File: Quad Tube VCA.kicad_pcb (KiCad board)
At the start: 2 copper layers, 162.6 x 100.3 mm, 212 parts, among them IC1 TL072, IC2 LM358, IC3 TL072, IC4 LM358, IC5 TL072, IC6 LM358, IC7 TL072, IC8 LM358

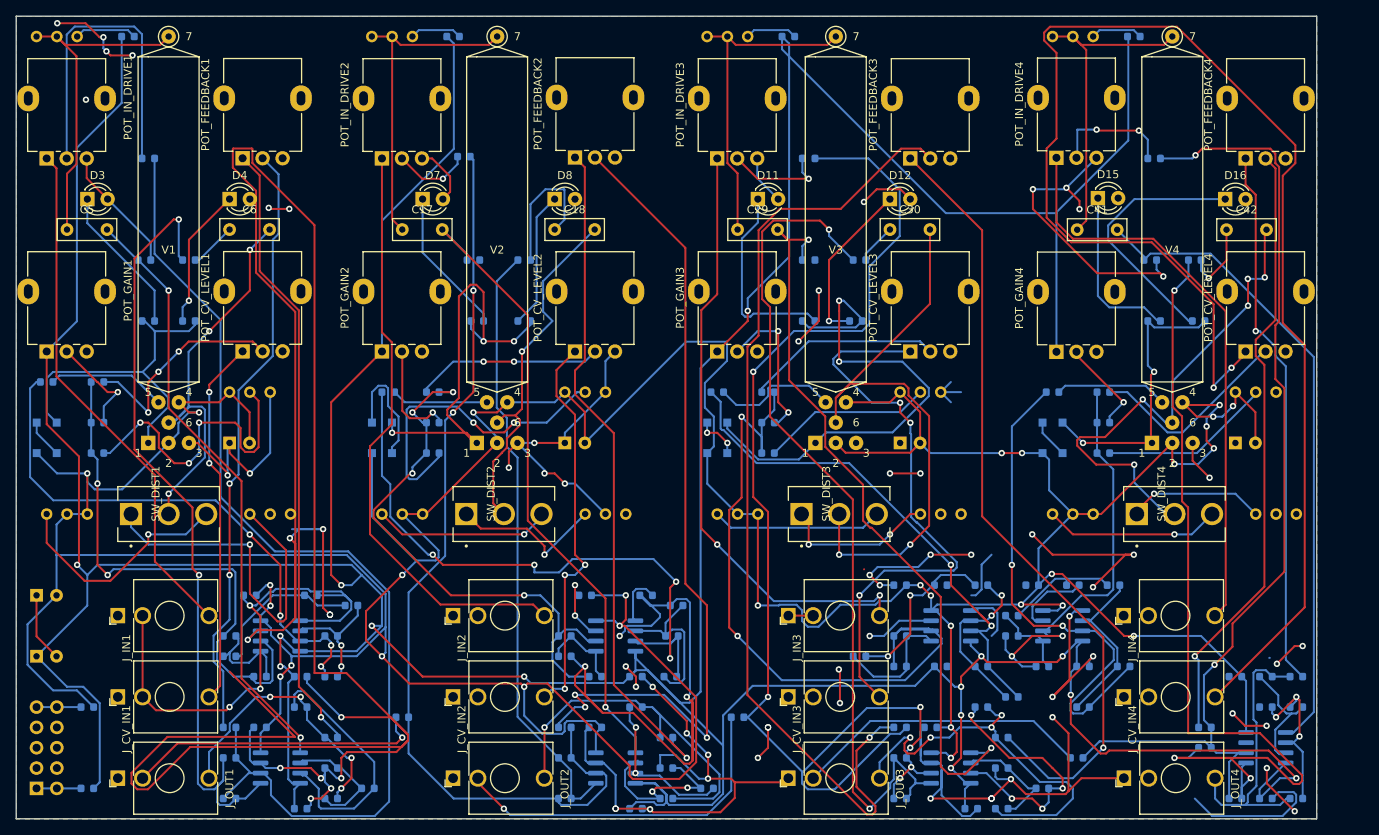
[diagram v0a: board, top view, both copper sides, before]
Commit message: power and vca1 routed
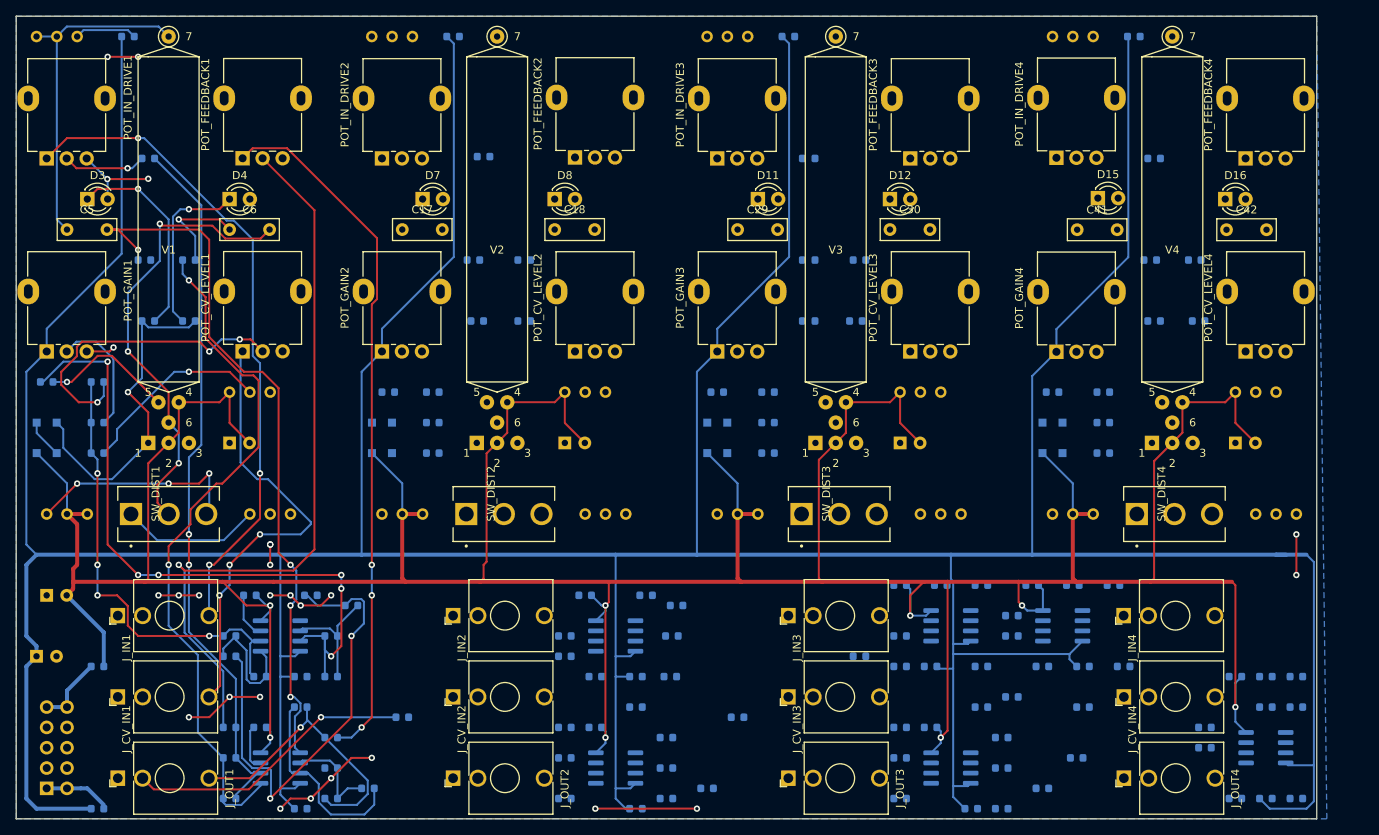
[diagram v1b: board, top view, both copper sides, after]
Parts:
- moved FB2 5.24 mm to (76.2, 125.7)
- moved FB1 2.84 mm to (76.2, 143.5), turned to 180 degrees
- moved R27 2.46 mm to (124.5, 62.0)
- moved C35 1.27 mm to (180.3, 125.7), turned to 180 degrees
- moved C3 1.27 mm to (69.8, 116.8)
- moved JP1 1.27 mm to (69.8, 141.0)
- turned R3 to 180 degrees
- turned R5 to 180 degrees
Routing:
- net GND: track 852.1 -> 88.2 mm, vias 74 -> 26
- net Net-(J_CV_IN4-Pad3): track 179.5 -> 0.00 mm, vias 2 -> 0
- net Net-(C27-Pad2): track 155.0 -> 0.00 mm, vias 6 -> 0
- net -12V: track 649.3 -> 523.6 mm, vias 30 -> 8
- net Net-(C39-Pad2): track 123.8 -> 0.00 mm, vias 2 -> 0
- net Net-(POT_FEEDBACK3-Pad2): track 121.7 -> 0.00 mm, vias 1 -> 0
- net Net-(C39-Pad1): track 117.2 -> 0.00 mm, vias 3 -> 0
- net Net-(C15-Pad2): track 117.2 -> 0.00 mm, vias 2 -> 0
- net Net-(C27-Pad1): track 108.4 -> 0.00 mm, vias 2 -> 0
- net Net-(POT_FEEDBACK2-Pad2): track 103.7 -> 0.00 mm, vias 3 -> 0
- net Net-(POT_FEEDBACK3-Pad1): track 99.2 -> 0.00 mm, vias 1 -> 0
- net Net-(C29-Pad2): track 93.8 -> 0.00 mm, vias 2 -> 0
- net Net-(C33-Pad1): track 88.4 -> 0.00 mm, vias 2 -> 0
- net Net-(POT_FEEDBACK2-Pad1): track 85.1 -> 0.00 mm, vias 1 -> 0
- net Net-(C20-Pad2): track 81.2 -> 0.00 mm, vias 4 -> 0
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
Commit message: changes footprints for pots/jacks
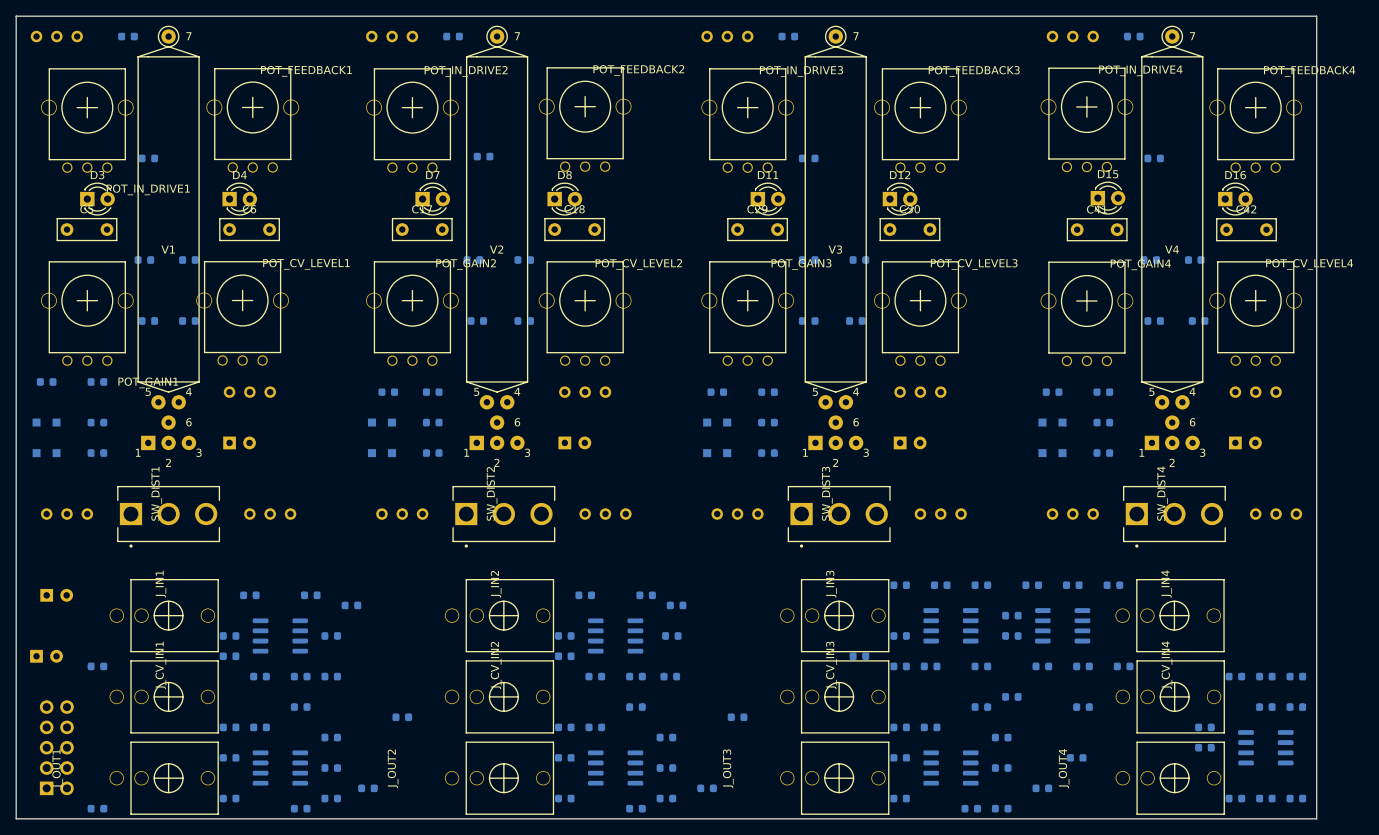
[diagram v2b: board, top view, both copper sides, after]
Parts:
- J_CV_IN1, J_CV_IN2, J_CV_IN3, J_CV_IN4, J_IN1, J_IN2, J_IN3, J_IN4, J_OUT1, J_OUT2, J_OUT3, J_OUT4: footprint Connector_Audio:Jack_3.5mm_QingPu_WQP-PJ398SM_Vertical_CircularHoles -> Eurocad:PJ301M-12
- POT_CV_LEVEL1, POT_CV_LEVEL2, POT_CV_LEVEL3, POT_CV_LEVEL4, POT_FEEDBACK1, POT_FEEDBACK2, POT_FEEDBACK3, POT_FEEDBACK4, POT_GAIN1, POT_GAIN2, POT_GAIN3, POT_GAIN4, POT_IN_DRIVE1, POT_IN_DRIVE2, POT_IN_DRIVE3, POT_IN_DRIVE4: footprint Potentiometer_THT:Potentiometer_Alpha_RD901F-40-00D_Single_Vertical -> Eurocad:Alpha9mmPot
- moved POT_GAIN1 8.13 mm to (74.9, 80.0), turned to 0 degrees
- moved POT_IN_DRIVE1 8.13 mm to (74.9, 55.9), turned to 0 degrees
- moved POT_GAIN4 7.41 mm to (199.9, 80.0), turned to 0 degrees
- moved POT_IN_DRIVE4 7.41 mm to (199.9, 55.8), turned to 0 degrees
- moved POT_GAIN3 7.41 mm to (157.5, 80.0), turned to 0 degrees
- moved POT_IN_DRIVE3 7.41 mm to (157.5, 55.9), turned to 0 degrees
- moved POT_GAIN2 7.41 mm to (115.6, 80.0), turned to 0 degrees
- moved POT_IN_DRIVE2 7.41 mm to (115.6, 55.9), turned to 0 degrees
- moved POT_FEEDBACK2 6.48 mm to (137.2, 55.8), turned to 0 degrees
- moved POT_FEEDBACK1 6.48 mm to (95.6, 55.9), turned to 0 degrees
- moved POT_CV_LEVEL2 6.48 mm to (137.2, 80.0), turned to 0 degrees
- moved POT_CV_LEVEL3 6.48 mm to (179.1, 80.0), turned to 0 degrees
- moved POT_CV_LEVEL4 6.48 mm to (221.0, 80.0), turned to 0 degrees
- moved POT_FEEDBACK3 6.48 mm to (179.1, 55.9), turned to 0 degrees
- moved POT_FEEDBACK4 6.48 mm to (221.0, 55.9), turned to 0 degrees
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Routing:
- net +12V: track 663.4 -> 0.00 mm
- net -12V: track 523.6 -> 0.00 mm, vias 8 -> 0
- net Net-(POT_FEEDBACK1-Pad2): track 92.6 -> 0.00 mm, vias 1 -> 0
- net Net-(C5-Pad2): track 91.1 -> 0.00 mm, vias 4 -> 0
- net Net-(C1-Pad2): track 89.0 -> 0.00 mm, vias 2 -> 0
- net GND: track 88.2 -> 0.00 mm, vias 26 -> 0
- net Net-(POT_FEEDBACK1-Pad1): track 87.5 -> 0.00 mm, vias 3 -> 0
- net Net-(C1-Pad1): track 86.5 -> 0.00 mm, vias 2 -> 0
- net Net-(C8-Pad2): track 85.1 -> 0.00 mm, vias 6 -> 0
- net Net-(J_IN1-Pad3): track 82.4 -> 0.00 mm, vias 3 -> 0
- net Net-(C14-Pad1): track 58.7 -> 0.00 mm, vias 2 -> 0
- net Net-(C6-Pad2): track 57.2 -> 0.00 mm, vias 3 -> 0
- net Net-(C9-Pad1): track 56.6 -> 0.00 mm, vias 4 -> 0
- net Net-(J_CV_IN1-Pad3): track 56.1 -> 0.00 mm, vias 3 -> 0
- net Net-(C5-Pad1): track 42.2 -> 0.00 mm
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- removed copper zone on B.Cu, net GND

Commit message: upadtes 3d models, makes more space at pcb edges
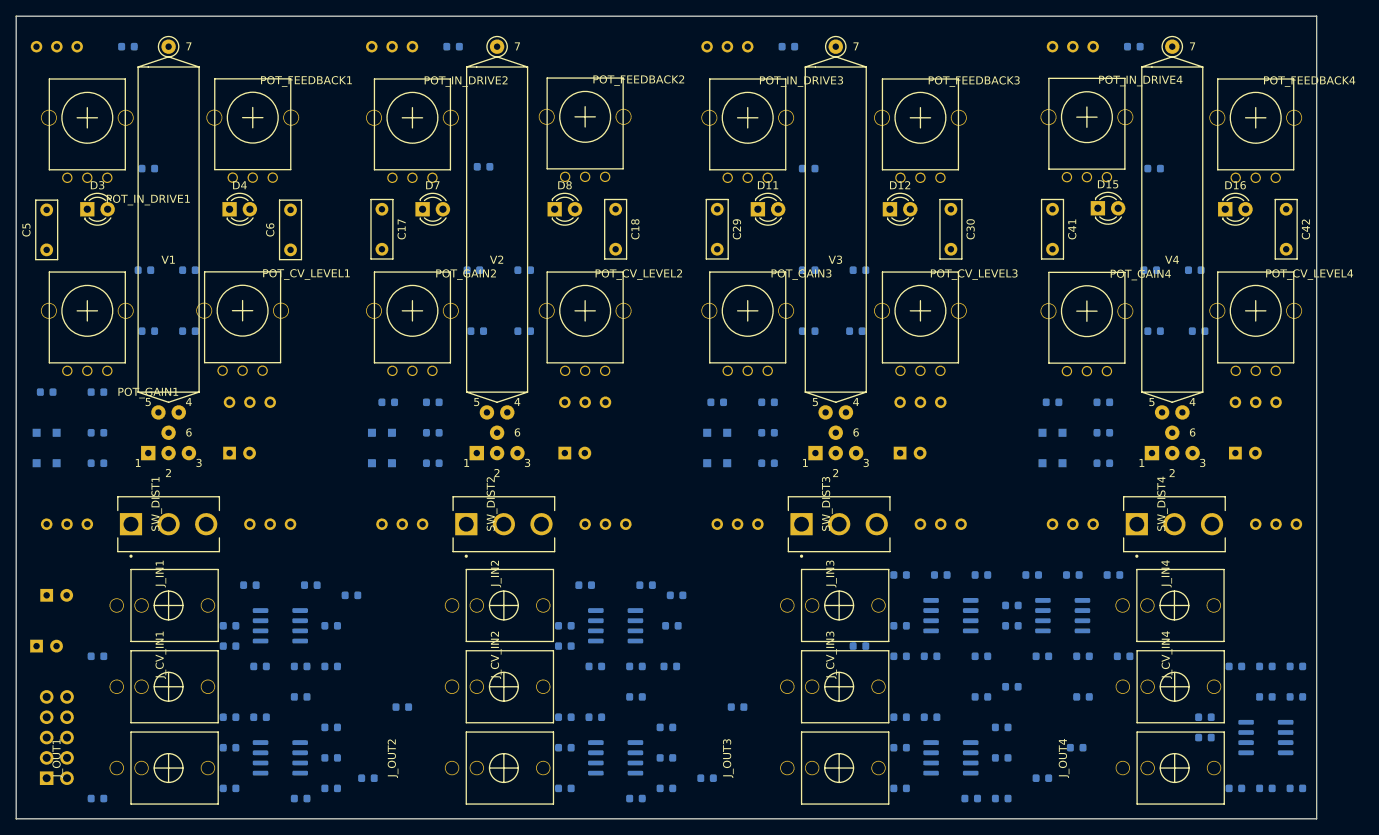
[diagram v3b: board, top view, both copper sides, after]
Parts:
- moved C18 8.03 mm to (141.0, 68.6), turned to 270 degrees
- moved C30 8.03 mm to (182.9, 68.6), turned to 270 degrees
- moved C6 8.03 mm to (100.3, 73.7), turned to 90 degrees
- moved C42 7.89 mm to (224.8, 68.6), turned to 270 degrees
- moved C41 4.00 mm to (195.6, 68.6), turned to 270 degrees
- moved C29 3.59 mm to (153.7, 68.6), turned to 270 degrees
- moved C17 3.59 mm to (111.8, 68.6), turned to 270 degrees
- moved C5 3.59 mm to (69.8, 73.7), turned to 90 degrees
- moved C1 1.27 mm to (92.7, 135.9)
- moved C13 1.27 mm to (95.2, 115.6)
- moved C14 1.27 mm to (102.9, 115.6)
- moved C15 1.27 mm to (134.6, 135.9)
- moved C16 1.27 mm to (152.4, 139.7)
- moved C25 1.27 mm to (137.2, 115.6)
- moved C26 1.27 mm to (144.8, 115.6)
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
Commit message: updates layout
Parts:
- moved R82 5.24 mm to (157.5, 135.9)
- moved R81 5.08 mm to (114.3, 135.9)
- moved R19 2.54 mm to (92.7, 125.7)
- moved R39 2.54 mm to (134.6, 125.7)
- moved R38 2.06 mm to (110.5, 92.7)
- moved R27 1.29 mm to (123.2, 63.5)
- moved C8 1.27 mm to (106.7, 120.7)
- moved D10 1.27 mm to (110.5, 100.3)
- moved D17 1.27 mm to (194.3, 96.5)
- moved D18 1.27 mm to (194.3, 100.3)
- moved D5 1.27 mm to (69.8, 97.8)
- moved D9 1.27 mm to (110.5, 96.5)
- moved R14 1.27 mm to (76.2, 97.8)
- moved R15 1.27 mm to (106.7, 125.7)
- moved R21 1.27 mm to (148.6, 133.3)
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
